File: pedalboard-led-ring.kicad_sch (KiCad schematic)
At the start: 33 parts, among them J1 middle, J2 edge

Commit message: Simplificaitons
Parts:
- removed H1, H2, H3: MountingHole, MountingHole:MountingHole_2.2mm_M2, symbol Mechanical:MountingHole
- removed J2: edge, Connector_PinSocket_2.00mm:PinSocket_2x02_P2.00mm_Vertical_SMD, symbol Connector_Generic:Conn_02x02_Odd_Even
- removed R2: 0, Resistor_SMD:R_0201_0603Metric_Pad0.64x0.40mm_HandSolder, symbol Device:R
- added JP1: SJ, Jumper:SolderJumper-2_P1.3mm_Bridged_RoundedPad1.0x1.5mm, symbol Jumper:SolderJumper_2_Bridged
- J1: now fitted
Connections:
- net VCC: now also JP1.2 (B)
- net at C1.1, D1.2 (VDD), D13.1 (K): now also JP1.1 (A)

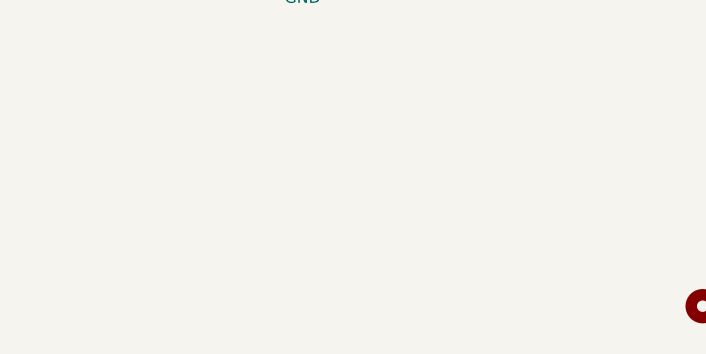
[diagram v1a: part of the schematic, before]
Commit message: Add fiducials for p&p
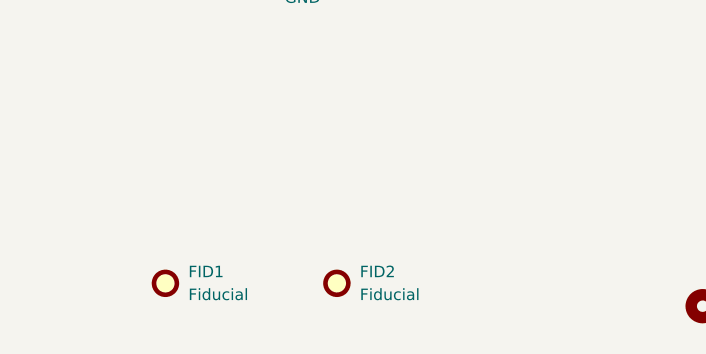
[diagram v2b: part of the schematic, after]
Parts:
- added FID1, FID2: Fiducial, Fiducial:Fiducial_0.5mm_Mask1mm, symbol Mechanical:Fiducial
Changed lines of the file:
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@@
+    )
+  )
+  (symbol (lib_id "Mechanical:Fiducial") (at 49.53 182.88 0) (unit 1)
+    (in_bom yes) (on_board yes) (dnp no) (fields_autoplaced)
+    (property "Reference" "FID2" (at 52.07 181.61 0)
+      (effects (font (size 1.27 1.27)) (justify left))
+    )
+    (property "Value" "Fiducial" (at 52.07 184.15 0)
+      (effects (font (size 1.27 1.27)) (justify left))
+    )
+    (property "Footprint" "Fiducial:Fiducial_0.5mm_Mask1mm" (at 49.53 182.88 0)
+      (effects (font (size 1.27 1.27)) hide)
+    )
+    (property "Datasheet" "~" (at 49.53 182.88 0)
+      (effects (font (size 1.27 1.27)) hide)
+    )
+    (instances
+      (project "pedalboard-led-ring"
+        (path "/02aefeb1-bdda-4e04-a64a-6cb1fcf66702"
+          (reference "FID2") (unit 1)
+        )
+      )
     )
   )
@@
         )
       )
+    )
+  )
+  (symbol (lib_id "Mechanical:Fiducial") (at 30.48 182.88 0) (unit 1)
+    (in_bom yes) (on_board yes) (dnp no) (fields_autoplaced)
+    (property "Reference" "FID1" (at 33.02 181.61 0)
+      (effects (font (size 1.27 1.27)) (justify left))
+    )
+    (property "Value" "Fiducial" (at 33.02 184.15 0)
+      (effects (font (size 1.27 1.27)) (justify left))
+    )
+    (property "Footprint" "Fiducial:Fiducial_0.5mm_Mask1mm" (at 30.48 182.88 0)
+      (effects (font (size 1.27 1.27)) hide)
+    )
+    (property "Datasheet" "~" (at 30.48 182.88 0)
+      (effects (font (size 1.27 1.27)) hide)
+    )
+    (instances
+      (project "pedalboard-led-ring"
+        (path "/02aefeb1-bdda-4e04-a64a-6cb1fcf66702"
+          (reference "FID1") (unit 1)
+        )
+      )

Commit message: Change to 0402 components
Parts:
- C1, C10, C11, C12, C2, C3, C4, C5, C6, C7, C8, C9: footprint Capacitor_SMD:C_0201_0603Metric_Pad0.64x0.40mm_HandSolder -> Capacitor_SMD:C_0402_1005Metric
- J1: value middle -> 02x02
- R1: footprint Resistor_SMD:R_0201_0603Metric_Pad0.64x0.40mm_HandSolder -> Resistor_SMD:R_0402_1005Metric
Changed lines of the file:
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@@
       (effects (font (size 1.27 1.27)) (justify left))
     )
-    (property "Footprint" "Capacitor_SMD:C_0201_0603Metric_Pad0.64x0.40mm_HandSolder" (at 91.1352 134.62 0)
+    (property "Footprint" "Capacitor_SMD:C_0402_1005Metric" (at 91.1352 134.62 0)
       (effects (font (size 1.27 1.27)) hide)
     )
@@
       (effects (font (size 1.27 1.27)) (justify left))
     )
-    (property "Footprint" "Capacitor_SMD:C_0201_0603Metric_Pad0.64x0.40mm_HandSolder" (at 35.2552 134.62 0)
+    (property "Footprint" "Capacitor_SMD:C_0402_1005Metric" (at 35.2552 134.62 0)
       (effects (font (size 1.27 1.27)) hide)
     )
@@
       (effects (font (size 1.27 1.27)) (justify left))
     )
-    (property "Footprint" "Capacitor_SMD:C_0201_0603Metric_Pad0.64x0.40mm_HandSolder" (at 21.2852 45.72 0)
+    (property "Footprint" "Capacitor_SMD:C_0402_1005Metric" (at 21.2852 45.72 0)
       (effects (font (size 1.27 1.27)) hide)
     )
@@
       (effects (font (size 1.27 1.27)) (justify left))
     )
-    (property "Footprint" "Capacitor_SMD:C_0201_0603Metric_Pad0.64x0.40mm_HandSolder" (at 147.0152 134.62 0)
+    (property "Footprint" "Capacitor_SMD:C_0402_1005Metric" (at 147.0152 134.62 0)
       (effects (font (size 1.27 1.27)) hide)
     )
@@
       (effects (font (size 1.27 1.27)) (justify left))
     )
-    (property "Value" "middle" (at 21.59 93.345 90)
+    (property "Value" "02x02" (at 21.59 93.345 90)
       (effects (font (size 1.27 1.27)) (justify left))
     )
@@
       (effects (font (size 1.27 1.27)) (justify left))
     )
-    (property "Footprint" "Capacitor_SMD:C_0201_0603Metric_Pad0.64x0.40mm_HandSolder" (at 113.9952 134.62 0)
+    (property "Footprint" "Capacitor_SMD:C_0402_1005Metric" (at 113.9952 134.62 0)
       (effects (font (size 1.27 1.27)) hide)
     )
@@
       (effects (font (size 1.27 1.27)) (justify left))
     )
-    (property "Footprint" "Capacitor_SMD:C_0201_0603Metric_Pad0.64x0.40mm_HandSolder" (at 68.2752 134.62 0)
+    (property "Footprint" "Capacitor_SMD:C_0402_1005Metric" (at 68.2752 134.62 0)
       (effects (font (size 1.27 1.27)) hide)
     )
@@
       (effects (font (size 1.27 1.27)) (justify left))
     )
-    (property "Footprint" "Capacitor_SMD:C_0201_0603Metric_Pad0.64x0.40mm_HandSolder" (at 102.5652 134.62 0)
+    (property "Footprint" "Capacitor_SMD:C_0402_1005Metric" (at 102.5652 134.62 0)
       (effects (font (size 1.27 1.27)) hide)
     )
@@
       (effects (font (size 1.27 1.27)) (justify left))
     )
-    (property "Footprint" "Capacitor_SMD:C_0201_0603Metric_Pad0.64x0.40mm_HandSolder" (at 135.5852 134.62 0)
+    (property "Footprint" "Capacitor_SMD:C_0402_1005Metric" (at 135.5852 134.62 0)
       (effects (font (size 1.27 1.27)) hide)
     )
@@
       (effects (font (size 1.27 1.27)) (justify left))
     )
-    (property "Footprint" "Resistor_SMD:R_0201_0603Metric_Pad0.64x0.40mm_HandSolder" (at 14.732 67.31 90)
+    (property "Footprint" "Resistor_SMD:R_0402_1005Metric" (at 14.732 67.31 90)
       (effects (font (size 1.27 1.27)) hide)
     )
@@
       (effects (font (size 1.27 1.27)) (justify left))
     )
-    (property "Footprint" "Capacitor_SMD:C_0201_0603Metric_Pad0.64x0.40mm_HandSolder" (at 56.8452 134.62 0)
+    (property "Footprint" "Capacitor_SMD:C_0402_1005Metric" (at 56.8452 134.62 0)
       (effects (font (size 1.27 1.27)) hide)
     )
@@
       (effects (font (size 1.27 1.27)) (justify left))
     )
-    (property "Footprint" "Capacitor_SMD:C_0201_0603Metric_Pad0.64x0.40mm_HandSolder" (at 124.1552 134.62 0)
+    (property "Footprint" "Capacitor_SMD:C_0402_1005Metric" (at 124.1552 134.62 0)
       (effects (font (size 1.27 1.27)) hide)
     )
@@
       (effects (font (size 1.27 1.27)) (justify left))
     )
-    (property "Footprint" "Capacitor_SMD:C_0201_0603Metric_Pad0.64x0.40mm_HandSolder" (at 79.7052 134.62 0)
+    (property "Footprint" "Capacitor_SMD:C_0402_1005Metric" (at 79.7052 134.62 0)
       (effects (font (size 1.27 1.27)) hide)
     )
@@
       (effects (font (size 1.27 1.27)) (justify left))
     )
-    (property "Footprint" "Capacitor_SMD:C_0201_0603Metric_Pad0.64x0.40mm_HandSolder" (at 46.6852 134.62 0)
-      (effects (font (size 1.27 1.27)) hide)
-    )
+    (property "Footprint" "Capacitor_SMD:C_0402_1005Metric" (at 46.6852 134.62 0)
+      (effects (font (size 1.27 1.27)) hide)
+    )

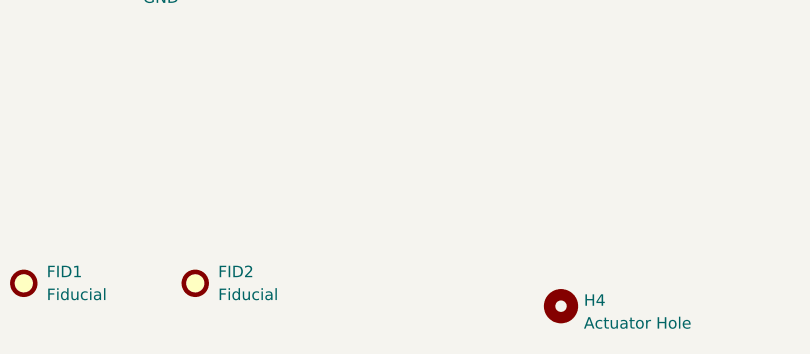
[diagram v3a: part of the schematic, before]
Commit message: Add additional Fiducial
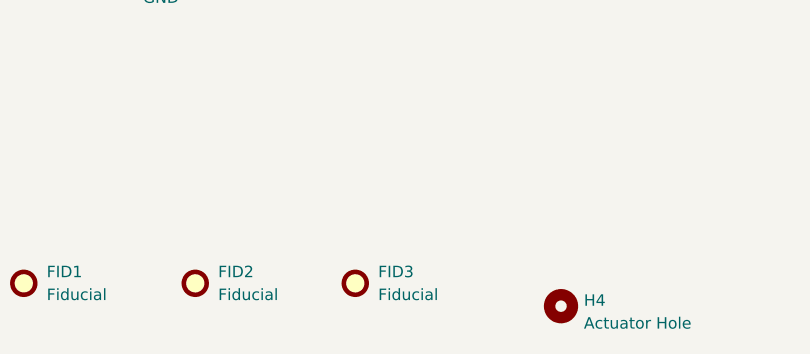
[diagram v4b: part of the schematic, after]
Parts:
- added FID3: Fiducial, Fiducial:Fiducial_0.5mm_Mask1mm, symbol Mechanical:Fiducial
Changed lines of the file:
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@@
+    )
+  )
+  (symbol (lib_id "Mechanical:Fiducial") (at 67.31 182.88 0) (unit 1)
+    (in_bom yes) (on_board yes) (dnp no) (fields_autoplaced)
+    (property "Reference" "FID3" (at 69.85 181.61 0)
+      (effects (font (size 1.27 1.27)) (justify left))
+    )
+    (property "Value" "Fiducial" (at 69.85 184.15 0)
+      (effects (font (size 1.27 1.27)) (justify left))
+    )
+    (property "Footprint" "Fiducial:Fiducial_0.5mm_Mask1mm" (at 67.31 182.88 0)
+      (effects (font (size 1.27 1.27)) hide)
+    )
+    (property "Datasheet" "~" (at 67.31 182.88 0)
+      (effects (font (size 1.27 1.27)) hide)
+    )
+    (instances
+      (project "pedalboard-led-ring"
+        (path "/02aefeb1-bdda-4e04-a64a-6cb1fcf66702"
+          (reference "FID3") (unit 1)
+        )
+      )
     )
   )

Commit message: Update BOM to 0402
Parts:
- C1, C10, C11, C12, C2, C3, C4, C5, C6, C7, C8, C9: Supplier https://www.digikey.ch/en/products/detail/samsung-electro-m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 -> https://www.digikey.ch/de/products/detail/samsung-electro-m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
- J1: Supplier https://www.digikey.ch/en/products/detail/gct/BF100-04-A-D-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 -> https://www.digikey.ch/en/products/detail/w%C3%BCrth-elektr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
- R1: Supplier https://www.digikey.ch/en/products/detail/panasonic-electro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 -> https://www.digikey.ch/en/products/detail/walsin-technology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

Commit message: Improve explaination text
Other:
- note added: "An optional hacky way of level conversion https://www.electrobob.com/ws2812-level-translator/"
- note removed: "A hacky way of level conversion https://www.electrobob.com/ws2812-level-translator/"
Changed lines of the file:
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@@
     (stroke (width 0) (type default))
   )
-  (text "A hacky way of level conversion\nhttps://www.electrobob.com/ws2812-level-translator/"
-    (at 59.69 24.13 0)
+  (text "An optional hacky way of level conversion\nhttps://www.electrobob.com/ws2812-level-translator/"
+    (at 57.15 30.48 0)
     (effects (font (size 1.27 1.27)) (justify left bottom))
   )
